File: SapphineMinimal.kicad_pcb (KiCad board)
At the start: 4 copper layers, 54.6 x 61 mm, 123 parts, among them IC201 DLHR-F50D-E1BD-C-NAV8, IC501 SLG59M1446V, J301 503182-1852, J401 Conn_01x01_Male, J501 JST, J801 USB_B_Micro, J802 Conn_02x05_Odd_Even, J803 Conn_02x05_Odd_Even, J805 Conn_01x04_Male, M701 AdafruitWINC1500, Q501 BC857BS, Q502 IRLML6402TRPBF, SW601 EVQP7C01P, SW801 EVQP7C01P, U201 LIS331DLHTR, U202 BMP388, U301 MB85RS1MT, U402 SAM-M8Q-0-10, U501 TPS62150, U601 DS3231SN, U801 ATSAMD21G18A-A

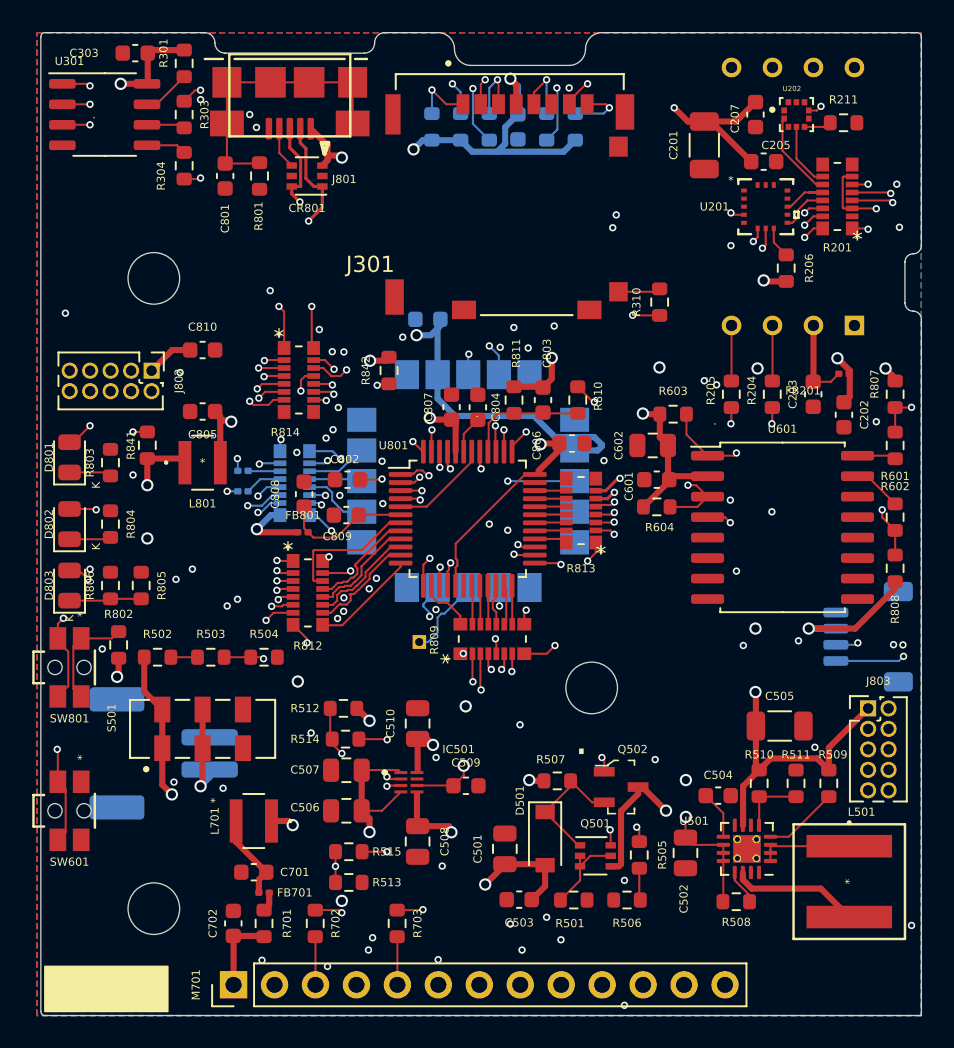
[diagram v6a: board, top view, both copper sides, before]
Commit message: Clean PCB but Added new clock to schematic
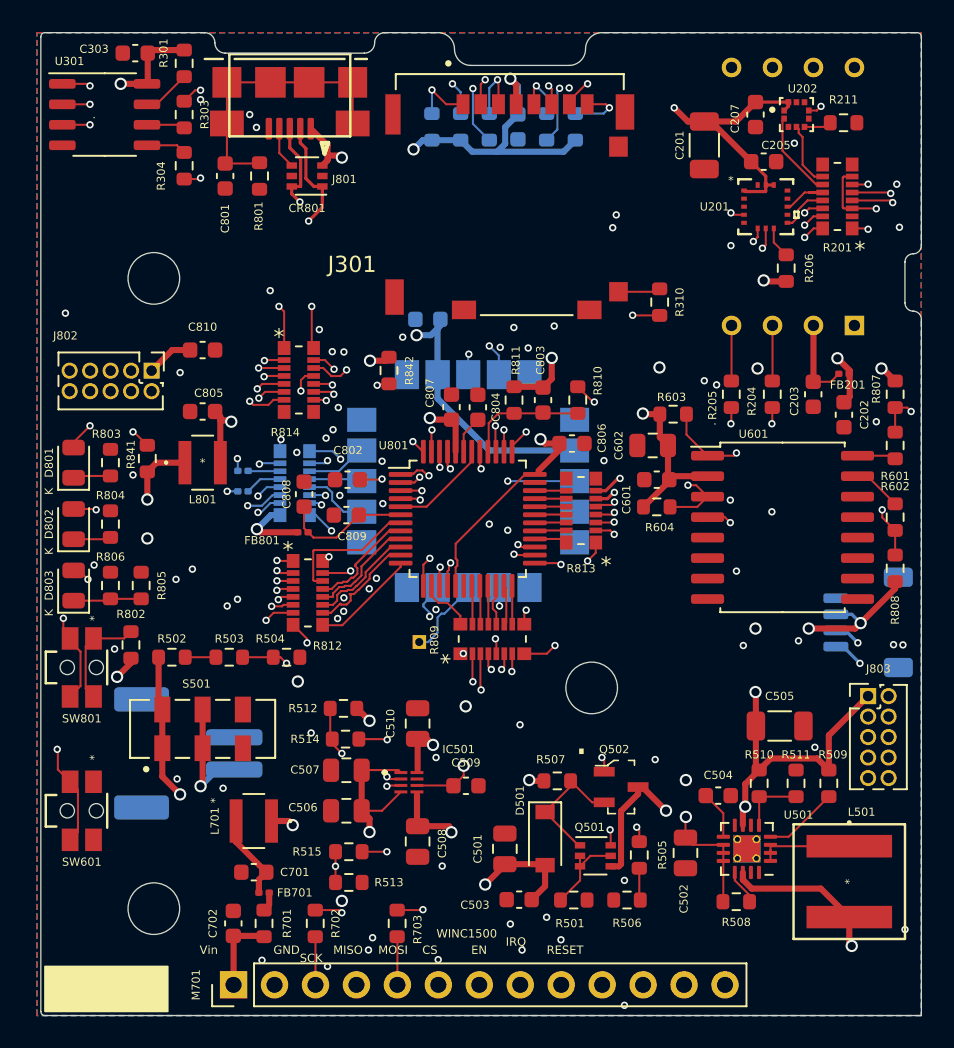
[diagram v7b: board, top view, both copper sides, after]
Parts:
- added G***: LOGO, Sapphire:SMU_Logo_Big, B.Cu at (120.7, 104.6)
- moved J501 1.52 mm to (86.1, 110.7)
- moved R504 1.40 mm to (92.2, 104.8)
- moved R503 1.14 mm to (88.6, 104.8)
- moved R502 0.89 mm to (85.1, 104.8)
- moved J805 0.89 mm to (128.3, 102.6)
- moved R841 0.83 mm to (83.6, 92.5)
- moved J803 0.76 mm to (128.3, 107.2)
- moved R802 0.76 mm to (82.5, 104.0)
- moved SW601 0.76 mm to (79.5, 114.3)
- moved SW801 0.76 mm to (79.5, 105.4)
- moved D801 0.42 mm to (79.0, 92.7)
- moved D802 0.25 mm to (79.0, 96.5)
- moved D803 0.25 mm to (79.0, 100.3)
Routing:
- net /P3V3: track 285.2 -> 306.4 mm, vias 23 -> 26
- net /SapphireMini_GNSS/GNSS_OUTPUT_POWER: track 57.0 -> 53.6 mm
- net Net-(J501-Pad1): track 6.07 -> 7.32 mm
- net GND: track 6.19 -> 7.40 mm, vias 0 -> 2
- net /SapphireMini_SD/SPI_SCK: track 123.4 -> 124.3 mm
- net /SapphireMini_Power/VBAT_MON: track 17.9 -> 17.0 mm
- net Net-(J301-Pad5): track 3.94 -> 3.18 mm
- net /SapphireMini_SD/SPI_MISO: track 136.0 -> 136.7 mm
- net /Sapphire_Proc/RESET: track 82.2 -> 82.9 mm
- net /Sapphire_Proc/RED_LED2: track 37.8 -> 37.1 mm
- net /SapphireMini_Power/VBAT: track 48.7 -> 48.0 mm
- net /SapphireMini_DLHR/I2C_SCL: track 93.3 -> 93.9 mm
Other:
- board text added: "+BAT"
- board text added: "CS"
- board text added: "EN"
- board text added: "GND"
- board text added: "IRQ"
- board text added: "MISO"
- board text added: "MOSI"
- board text added: "RESET"
- board text added: "SCK"
- board text added: "Vin"
- board text added: "WINC1500"
- board text added: "c hayward 10/3/2022"
- board text added: "stemma"

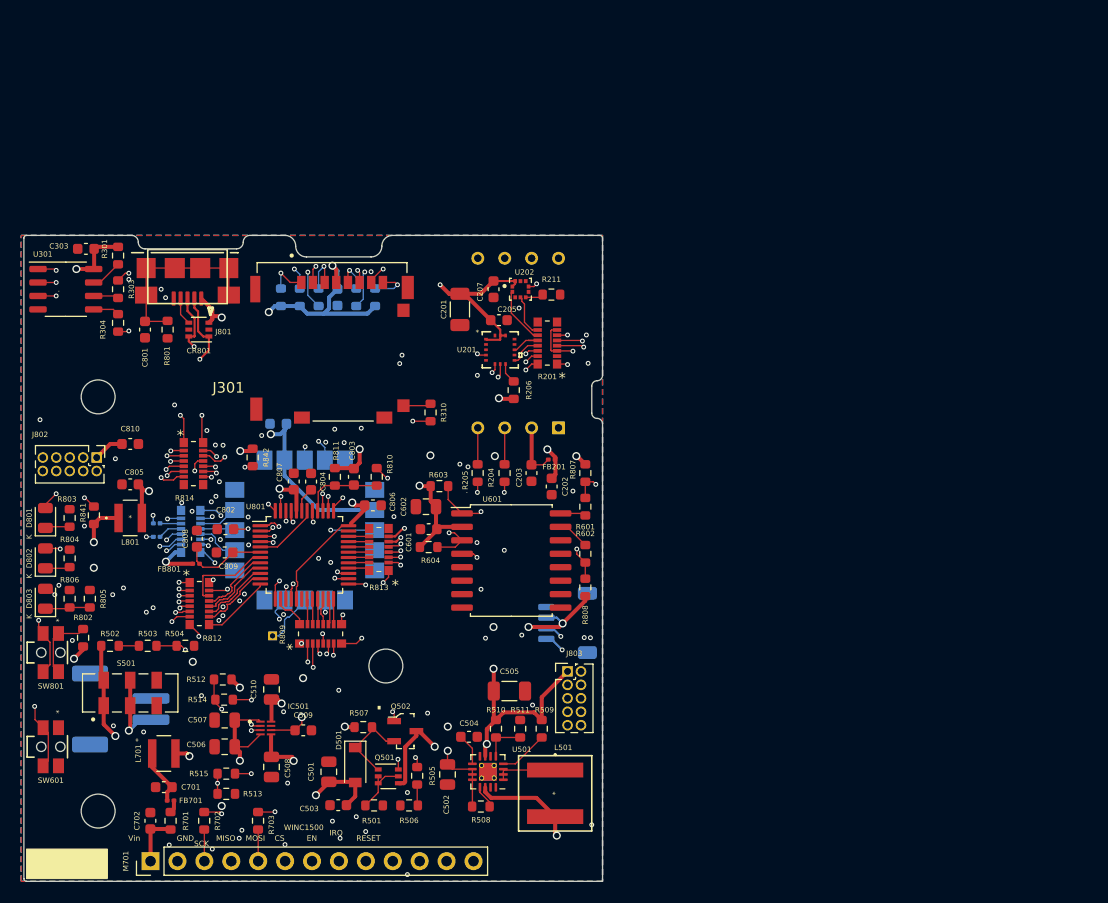
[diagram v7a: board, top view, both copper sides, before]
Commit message: Skematic updated for power and 1PSI sensor
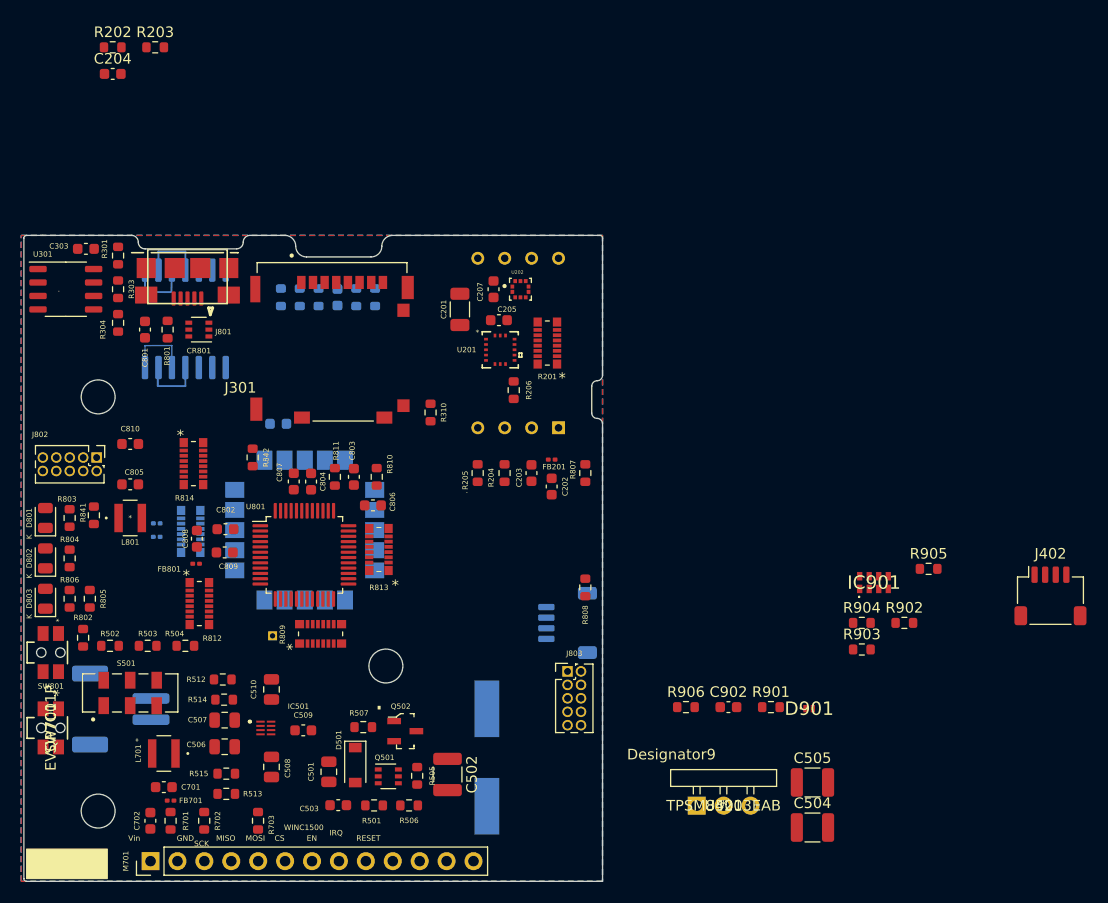
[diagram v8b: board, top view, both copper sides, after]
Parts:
- removed C601: 100nF, Capacitor_SMD:C_0603_1608Metric
- removed C602: 1uF, Capacitor_SMD:C_0805_2012Metric
- removed G***: LOGO, Sapphire:SMU_Logo_Big
- removed L501: L_Iron, SapphineMinimal:74439344022
- removed R211: 0, Resistor_SMD:R_0603_1608Metric
- removed R508, R509: 100K, Resistor_SMD:R_0603_1608Metric
- removed R510: 562K, Resistor_SMD:R_0603_1608Metric
- removed R511: 180K, Resistor_SMD:R_0603_1608Metric
- removed R601, R602: 47, Resistor_SMD:R_0603_1608Metric
- removed R603, R604: 47K5, Resistor_SMD:R_0603_1608Metric
- removed SW601: EVQP7C01P, Sapphire:EVQP7C01P
- removed U601: DS3231SN, Package_SO:SOIC-16W_7.5x10.3mm_P1.27mm
- added C204: 100nF, Capacitor_SMD:C_0603_1608Metric, F.Cu at (85.3, 50.8)
- added C901: FC0H224ZFTBR24, SamacSys_Parts:CAPAE1080X880N, B.Cu at (120.7, 115.3)
- added C902: 100nF, Capacitor_SMD:C_0603_1608Metric, F.Cu at (143.5, 110.6)
- added D901: BAS70L,315, SamacSys_Parts:PESD5V0S1BL315, F.Cu at (151.1, 110.7)
- added IC901: RV-8803-C7-32.768k-3PPM-TA-QA, SamacSys_Parts:RV8803C7, F.Cu at (157.2, 98.8)
- added J402: Conn_01x04_Male, Connector_JST:JST_SH_SM04B-SRSS-TB_1x04-1MP_P1.00mm_Horizontal, F.Cu at (173.8, 100.1)
- added R202: 47, Resistor_SMD:R_0603_1608Metric, F.Cu at (85.3, 48.3)
- added R203: 47, Resistor_SMD:R_0603_1608Metric, F.Cu at (89.4, 48.3)
- added R901: 330, Resistor_SMD:R_0603_1608Metric, F.Cu at (147.5, 110.6)
- added R902: 100K, Resistor_SMD:R_0603_1608Metric, F.Cu at (160.1, 102.6)
- added R903: 47, Resistor_SMD:R_0603_1608Metric, F.Cu at (156.0, 105.1)
- added R904: 47, Resistor_SMD:R_0603_1608Metric, F.Cu at (156.0, 102.6)
- added R905: 100K, Resistor_SMD:R_0603_1608Metric, F.Cu at (162.3, 97.5)
- added R906: 100K, Resistor_SMD:R_0603_1608Metric, F.Cu at (139.4, 110.6)
- added SW701: EVQP7C01P, Sapphire:EVQP7C01P, F.Cu at (79.5, 112.5)
- added U203: MS5525DSO, SapphineMinimal:TE_MS5525DSO-DBxxxyS, B.Cu at (92.2, 73.9)
- C502: value 10uF -> 47uF; footprint Capacitor_SMD:C_0805_2012Metric -> Capacitor_SMD:C_1210_3225Metric
- C504: value 390pF -> 10uF; footprint Capacitor_SMD:C_0603_1608Metric -> Capacitor_SMD:C_1210_3225Metric
- C505: value 22uF -> 47uF; footprint Capacitor_SMD:C_1206_3216Metric -> Capacitor_SMD:C_1210_3225Metric
- R811: value 2k2 -> 2K
- R841: value 1k0 -> 2K
- U202: value BMP388 -> BMP390
- U501: value TPS62150 -> TPSM84203EAB; footprint Package_DFN_QFN:VQFN-16-1EP_3x3mm_P0.5mm_EP1.68x1.68mm_ThermalVias -> Sapphire:TPSM84203EAB
- moved C504 33.5 mm to (151.4, 121.9)
- moved C505 29.9 mm to (151.4, 117.7)
- moved U501 22.5 mm to (143.0, 119.9), turned to 0 degrees
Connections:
- net /SapphireMini_DLHR/I2C_SCL renamed /I2C_SCL
- net /SapphireMini_DLHR/I2C_SDA renamed /I2C_SDA
- C401 pad 1: /SapphireMini_GNSS/GNSS_OUTPUT_POWER -> /P3V3
- C502 pad 1: /SapphireMini_Power/PWR_IN -> /P3V3
- C504 pad 1: Net-(C504-Pad1) -> /SapphireMini_Power/PWR_IN
- C508 pad 1: /SapphireMini_GNSS/GNSS_OUTPUT_POWER -> /P3V3
- IC501 pad 5: /SapphireMini_GNSS/GNSS_OUTPUT_POWER -> /P3V3
- R401 pad 11: /SapphireMini_GNSS/SAM_RXD -> /SapphireMini_GNSS/SAM_TXD
- R401 pad 12: /SapphireMini_GNSS/SAM_TXD -> /SapphireMini_GNSS/SAM_RXD
- R809 pad 1: /Sapphire_Proc/PB1 -> /Sapphire_Proc/SD_CD
- R809 pad 4: /SapphireMini_Power/VBAT_MON -> /Sapphire_Proc/AUX1
- R812 pad 5: /Sapphire_Proc/RS232_TXD5 -> /Sapphire_Proc/PB1
- R812 pad 6: /Sapphire_Proc/RS232_RXD5 -> /SapphireMini_Power/VBAT_MON
- R812 pad 7: /Sapphire_Proc/SD_CD -> /Sapphire_Proc/RS232_TXD5
- R812 pad 8: /Sapphire_Proc/AUX1 -> /Sapphire_Proc/RS232_RXD5
- R814 pad 4: /SapphireMini_DS3231/SQW -> /RV8803/SQW
- U202 pad 5: Net-(R211-Pad1) -> GND
- U402 pad 17: /SapphireMini_GNSS/GNSS_OUTPUT_POWER -> /P3V3
- U402 pad 2: /SapphireMini_GNSS/GNSS_OUTPUT_POWER -> /P3V3
- U501 pad 1: Net-(L501-Pad1) -> /SapphireMini_Power/PWR_IN
- U501 pad 2: Net-(L501-Pad1) -> GND
- U501 pad 3: Net-(L501-Pad1) -> /P3V3
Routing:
- net /P3V3: track 306.4 -> 0.00 mm, vias 26 -> 0
- net /SapphireMini_SD/SPI_MISO: track 136.7 -> 0.00 mm, vias 5 -> 0
- net /SapphireMini_SD/SPI_MOSI: track 131.6 -> 0.00 mm, vias 8 -> 0
- net /SapphireMini_SD/SPI_SCK: track 124.3 -> 0.00 mm, vias 8 -> 0
- net /I2C_SCL: track 93.9 -> 0.00 mm, vias 10 -> 0
- net /I2C_SDA: track 86.7 -> 0.00 mm, vias 8 -> 0
- net /Sapphire_Proc/GREEN_LED: track 83.9 -> 0.00 mm, vias 5 -> 0
- net /Sapphire_Proc/RESET: track 82.9 -> 0.00 mm, vias 4 -> 0
- net /Sapphire_Proc/RED_LED: track 78.2 -> 0.00 mm, vias 5 -> 0
- net /SapphireMini_Power/VBUS: track 66.9 -> 0.00 mm, vias 3 -> 0
- net /Sapphire_Proc/ACC_INT2: track 59.9 -> 0.00 mm, vias 3 -> 0
- net /SapphireMini_Power/SD_OUTPUT_POWER: track 59.6 -> 0.00 mm, vias 3 -> 0
- net /Sapphire_Proc/ACC_INT1: track 59.5 -> 0.00 mm, vias 3 -> 0
- net /SapphireMini_DLHR/BMP_INT: track 56.7 -> 0.00 mm, vias 3 -> 0
- net /Sapphire_Proc/WIFI_EN: track 54.8 -> 0.00 mm, vias 2 -> 0
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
